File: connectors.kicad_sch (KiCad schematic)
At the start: 4 parts, among them J2 Conn_01x02, J3 Conn_01x02, J6 Conn_01x04, J7 Conn_01x04

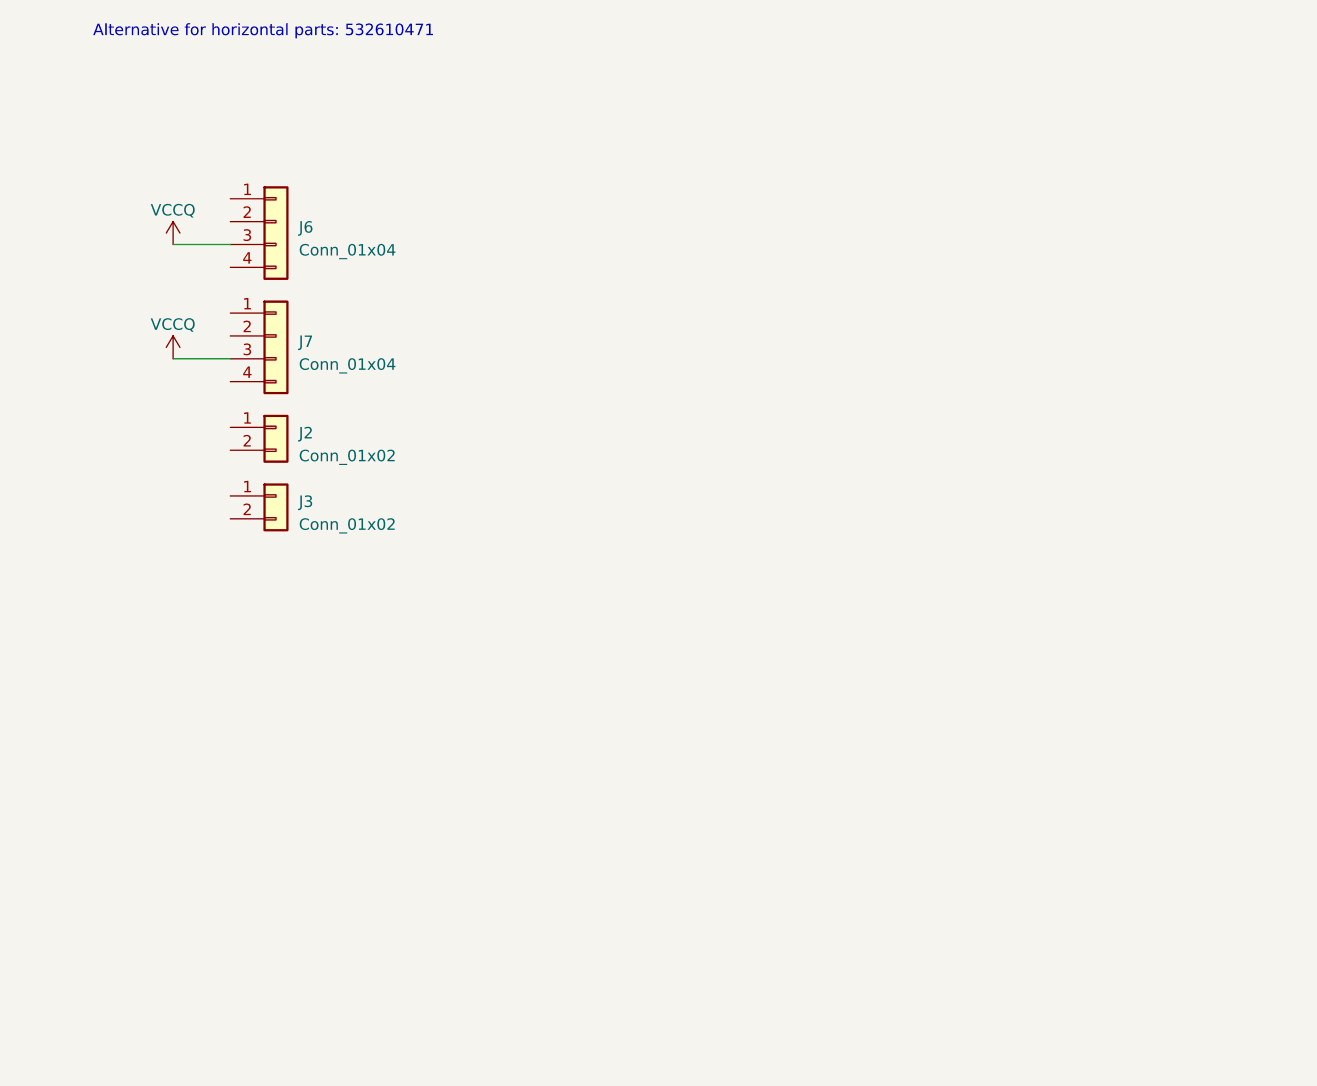
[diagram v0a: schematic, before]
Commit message: Add connections between existing sheets
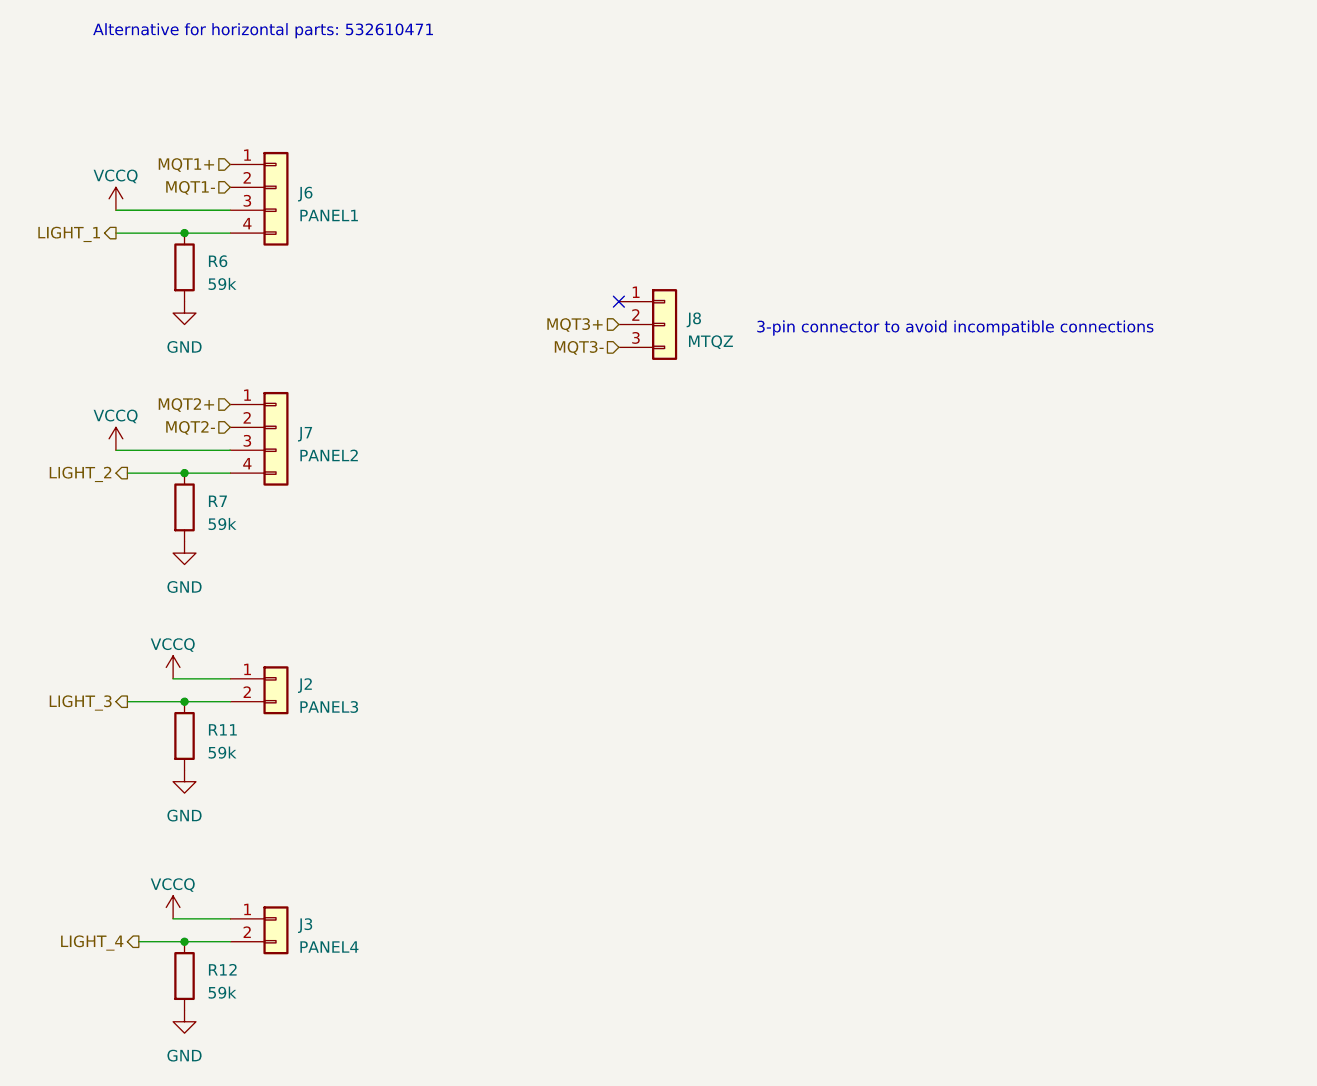
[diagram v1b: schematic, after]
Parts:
- added J8: MTQZ, Connector_Molex:Molex_PicoBlade_53398-0371_1x03-1MP_P1.25mm_Vertical, symbol Connector_Generic:Conn_01x03
- added R11, R12, R6, R7: 59k, LED_SMD:LED_0805_2012Metric_Pad1.15x1.40mm_HandSolder, symbol Device:R
- J2: value Conn_01x02 -> PANEL3; footprint (none) -> Connector_Molex:Molex_PicoBlade_53398-0271_1x02-1MP_P1.25mm_Vertical; MPN (none) -> 533980271
- J3: value Conn_01x02 -> PANEL4; footprint (none) -> Connector_Molex:Molex_PicoBlade_53398-0271_1x02-1MP_P1.25mm_Vertical; MPN (none) -> 533980271
- J6: value Conn_01x04 -> PANEL1; footprint (none) -> Connector_Molex:Molex_PicoBlade_53398-0471_1x04-1MP_P1.25mm_Vertical; MPN (none) -> 533980471
- J7: value Conn_01x04 -> PANEL2; footprint (none) -> Connector_Molex:Molex_PicoBlade_53398-0471_1x04-1MP_P1.25mm_Vertical; MPN (none) -> 533980471
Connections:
- net VCCQ: now also J2.1 (Pin_1), J3.1 (Pin_1)
- net MQT1+: now reaches J6.1 (Pin_1)
- net MQT1-: now reaches J6.2 (Pin_2)
- net LIGHT_1: now reaches J6.4 (Pin_4)
- net LIGHT_1: now also R6.1
- net LIGHT_3: now reaches J2.2 (Pin_2)
- net LIGHT_3: now also R11.1
- net MQT2+: now reaches J7.1 (Pin_1)
- net MQT2-: now reaches J7.2 (Pin_2)
- net LIGHT_2: now reaches J7.4 (Pin_4)
- net LIGHT_2: now also R7.1
- net LIGHT_4: now reaches J3.2 (Pin_2)
- net LIGHT_4: now also R12.1
- new net GND: R11.2, R12.2, R6.2, R7.2
- new net MQT3+: J8.2 (Pin_2)
- new net MQT3-: J8.3 (Pin_3)
- no-connect marks 0 -> 1
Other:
- note added: "3-pin connector to avoid incompatible connections"
- moved on the sheet: J2, J6

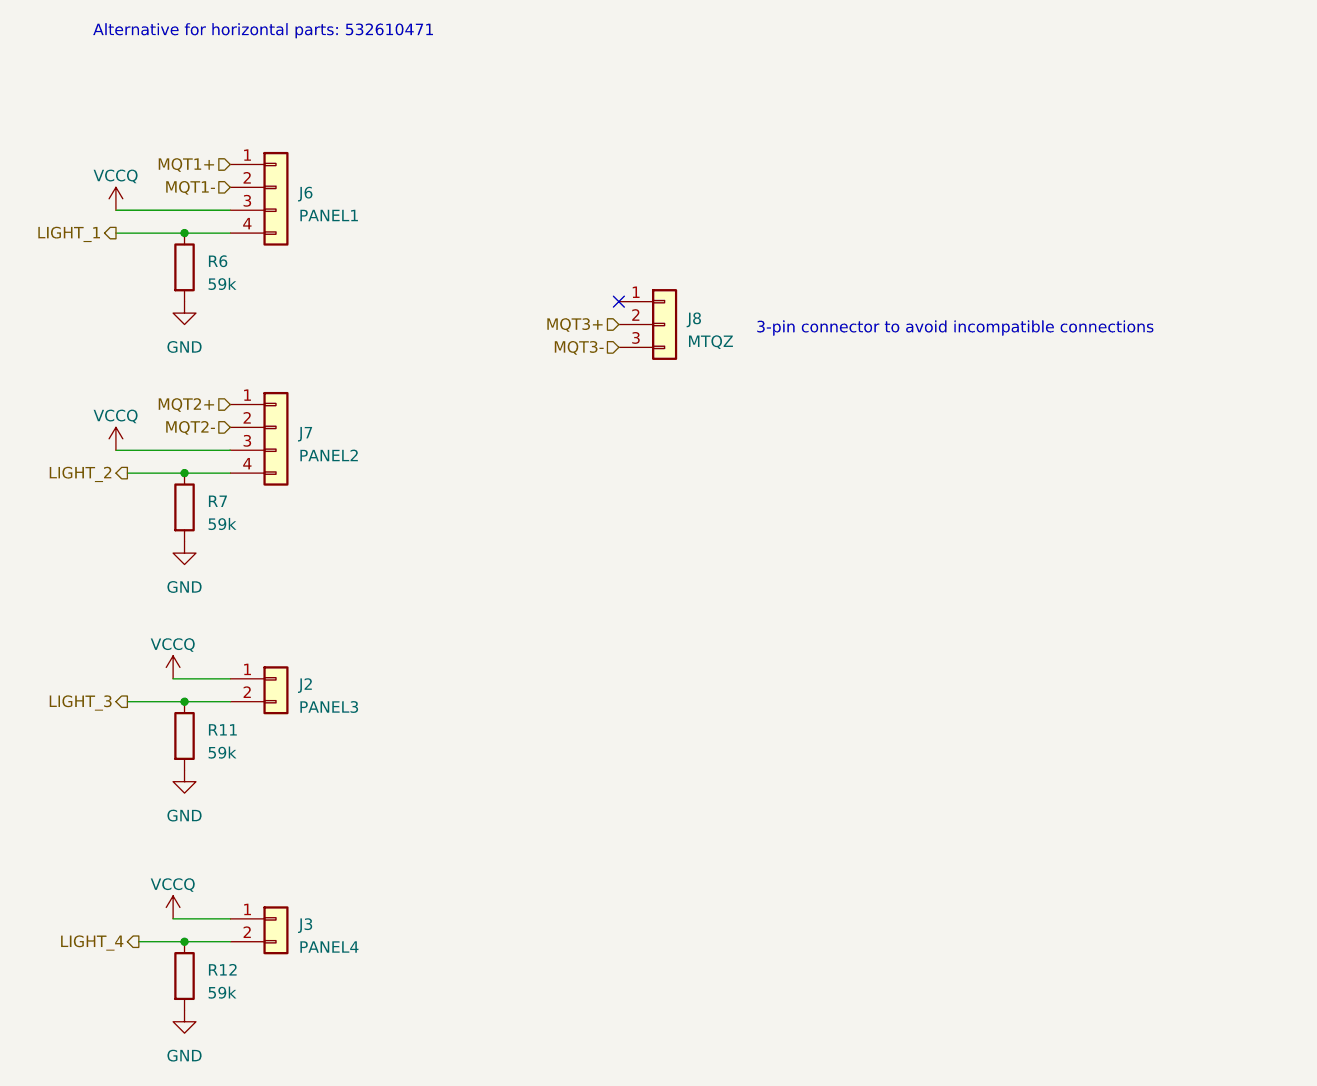
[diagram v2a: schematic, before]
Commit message: Reannotate schematic
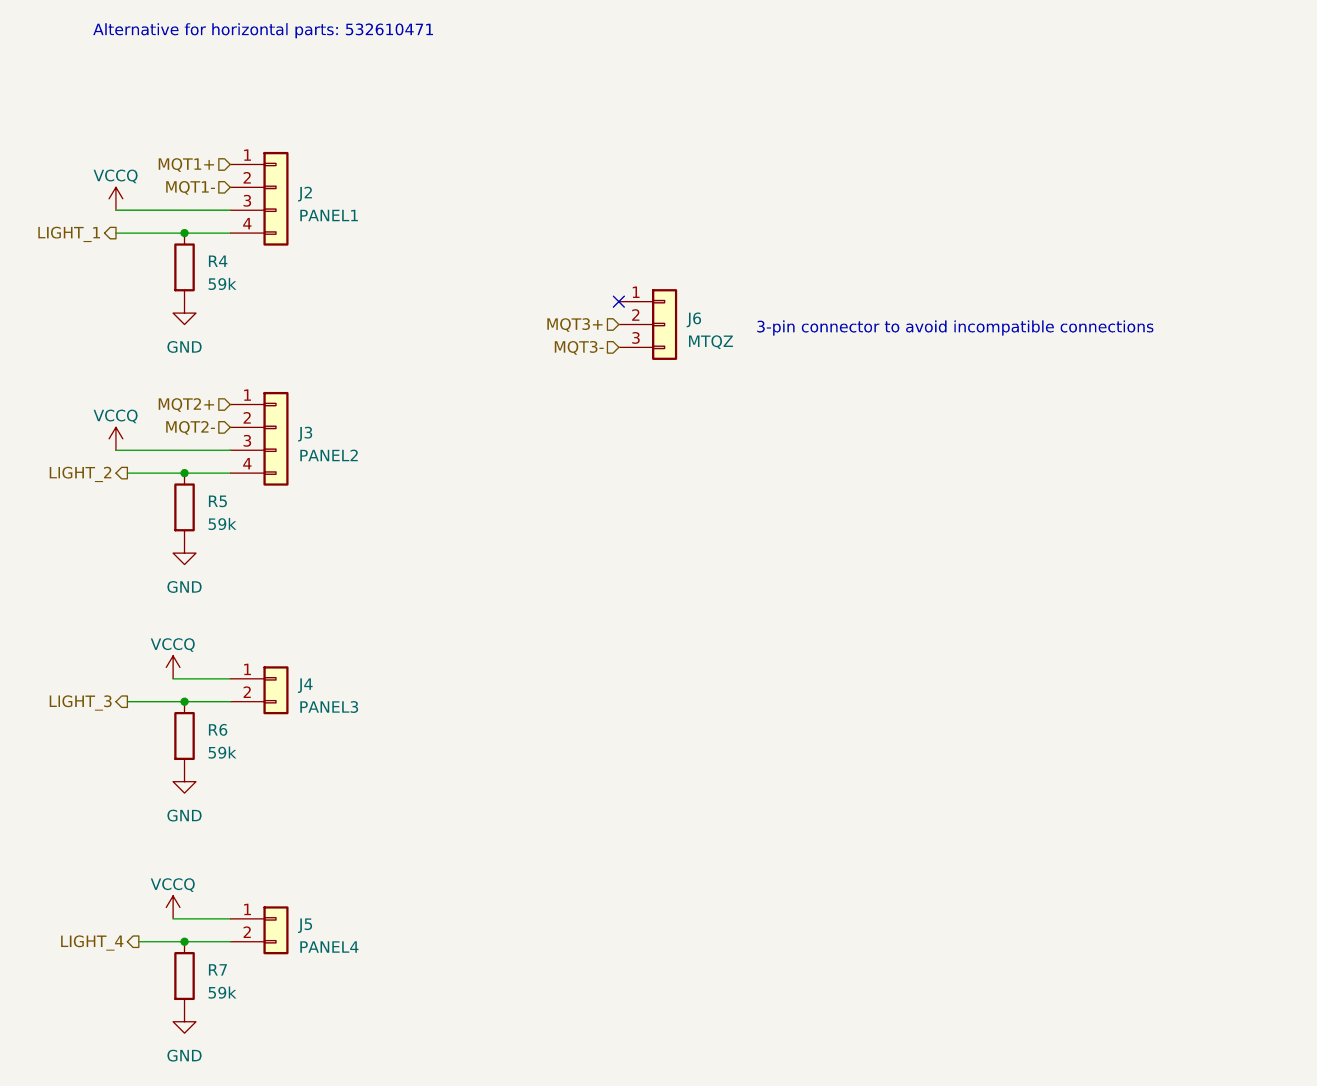
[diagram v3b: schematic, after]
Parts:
- renumbered J6 to J2, J7 to J3, J2 to J4, J3 to J5, J8 to J6, R6 to R4, R7 to R5, R11 to R6, R12 to R7
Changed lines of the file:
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@@
   (symbol (lib_id "Device:R") (at 116.84 67.31 0) (unit 1)
     (in_bom yes) (on_board yes) (dnp no) (fields_autoplaced)
-    (property "Reference" "R6" (at 119.38 66.675 0)
+    (property "Reference" "R4" (at 119.38 66.675 0)
       (effects (font (size 1.27 1.27)) (justify left))
     )
@@
       (project "NEW_PCB_ADCS"
         (path "/42c40d7d-71af-4ce9-bac9-d638f259c957/8584c500-e681-4774-8e2d-f320630e3d46"
-          (reference "R6") (unit 1)
+          (reference "R4") (unit 1)
         )
       )
@@
   (symbol (lib_id "Connector_Generic:Conn_01x03") (at 170.18 73.66 0) (unit 1)
     (in_bom yes) (on_board yes) (dnp no) (fields_autoplaced)
-    (property "Reference" "J8" (at 172.72 73.025 0)
+    (property "Reference" "J6" (at 172.72 73.025 0)
       (effects (font (size 1.27 1.27)) (justify left))
     )
@@
       (project "NEW_PCB_ADCS"
         (path "/42c40d7d-71af-4ce9-bac9-d638f259c957/8584c500-e681-4774-8e2d-f320630e3d46"
-          (reference "J8") (unit 1)
+          (reference "J6") (unit 1)
         )
       )
@@
   (symbol (lib_id "Connector_Generic:Conn_01x04") (at 127 58.42 0) (unit 1)
     (in_bom yes) (on_board yes) (dnp no) (fields_autoplaced)
-    (property "Reference" "J6" (at 129.54 59.055 0)
+    (property "Reference" "J2" (at 129.54 59.055 0)
       (effects (font (size 1.27 1.27)) (justify left))
     )
@@
       (project "NEW_PCB_ADCS"
         (path "/42c40d7d-71af-4ce9-bac9-d638f259c957/8584c500-e681-4774-8e2d-f320630e3d46"
-          (reference "J6") (unit 1)
+          (reference "J2") (unit 1)
         )
       )
@@
   (symbol (lib_id "Device:R") (at 116.84 146.05 0) (unit 1)
     (in_bom yes) (on_board yes) (dnp no) (fields_autoplaced)
-    (property "Reference" "R12" (at 119.38 145.415 0)
+    (property "Reference" "R7" (at 119.38 145.415 0)
       (effects (font (size 1.27 1.27)) (justify left))
     )
@@
       (project "NEW_PCB_ADCS"
         (path "/42c40d7d-71af-4ce9-bac9-d638f259c957/8584c500-e681-4774-8e2d-f320630e3d46"
-          (reference "R12") (unit 1)
+          (reference "R7") (unit 1)
         )
       )
@@
   (symbol (lib_id "Connector_Generic:Conn_01x02") (at 127 113.03 0) (unit 1)
     (in_bom yes) (on_board yes) (dnp no) (fields_autoplaced)
-    (property "Reference" "J2" (at 129.54 113.665 0)
+    (property "Reference" "J4" (at 129.54 113.665 0)
       (effects (font (size 1.27 1.27)) (justify left))
     )
@@
       (project "NEW_PCB_ADCS"
         (path "/42c40d7d-71af-4ce9-bac9-d638f259c957/8584c500-e681-4774-8e2d-f320630e3d46"
-          (reference "J2") (unit 1)
+          (reference "J4") (unit 1)
         )
       )
@@
   (symbol (lib_id "Connector_Generic:Conn_01x02") (at 127 139.7 0) (unit 1)
     (in_bom yes) (on_board yes) (dnp no) (fields_autoplaced)
-    (property "Reference" "J3" (at 129.54 140.335 0)
+    (property "Reference" "J5" (at 129.54 140.335 0)
       (effects (font (size 1.27 1.27)) (justify left))
     )
@@
       (project "NEW_PCB_ADCS"
         (path "/42c40d7d-71af-4ce9-bac9-d638f259c957/8584c500-e681-4774-8e2d-f320630e3d46"
-          (reference "J3") (unit 1)
+          (reference "J5") (unit 1)
         )
       )
@@
   (symbol (lib_id "power:GND") (at 116.84 123.19 0) (unit 1)
     (in_bom yes) (on_board yes) (dnp no) (fields_autoplaced)
-    (property "Reference" "#PWR061" (at 116.84 129.54 0)
+    (property "Reference" "#PWR015" (at 116.84 129.54 0)
       (effects (font (size 1.27 1.27)) hide)
     )
@@
       (project "NEW_PCB_ADCS"
         (path "/42c40d7d-71af-4ce9-bac9-d638f259c957/8584c500-e681-4774-8e2d-f320630e3d46"
-          (reference "#PWR061") (unit 1)
+          (reference "#PWR015") (unit 1)
         )
       )
@@
   (symbol (lib_id "power:VCCQ") (at 115.57 139.7 0) (unit 1)
     (in_bom yes) (on_board yes) (dnp no) (fields_autoplaced)
-    (property "Reference" "#PWR066" (at 115.57 143.51 0)
+    (property "Reference" "#PWR012" (at 115.57 143.51 0)
       (effects (font (size 1.27 1.27)) hide)
     )
@@
       (project "NEW_PCB_ADCS"
         (path "/42c40d7d-71af-4ce9-bac9-d638f259c957/8584c500-e681-4774-8e2d-f320630e3d46"
-          (reference "#PWR066") (unit 1)
+          (reference "#PWR012") (unit 1)
         )
       )
@@
   (symbol (lib_id "power:VCCQ") (at 109.22 87.63 0) (unit 1)
     (in_bom yes) (on_board yes) (dnp no) (fields_autoplaced)
-    (property "Reference" "#PWR065" (at 109.22 91.44 0)
+    (property "Reference" "#PWR010" (at 109.22 91.44 0)
       (effects (font (size 1.27 1.27)) hide)
     )
@@
       (project "NEW_PCB_ADCS"
         (path "/42c40d7d-71af-4ce9-bac9-d638f259c957/8584c500-e681-4774-8e2d-f320630e3d46"
-          (reference "#PWR065") (unit 1)
+          (reference "#PWR010") (unit 1)
         )
       )
@@
   (symbol (lib_id "power:VCCQ") (at 115.57 113.03 0) (unit 1)
     (in_bom yes) (on_board yes) (dnp no) (fields_autoplaced)
-    (property "Reference" "#PWR067" (at 115.57 116.84 0)
+    (property "Reference" "#PWR011" (at 115.57 116.84 0)
       (effects (font (size 1.27 1.27)) hide)
     )
@@
       (project "NEW_PCB_ADCS"
         (path "/42c40d7d-71af-4ce9-bac9-d638f259c957/8584c500-e681-4774-8e2d-f320630e3d46"
-          (reference "#PWR067") (unit 1)
+          (reference "#PWR011") (unit 1)
         )
       )
@@
   (symbol (lib_id "power:GND") (at 116.84 149.86 0) (unit 1)
     (in_bom yes) (on_board yes) (dnp no) (fields_autoplaced)
-    (property "Reference" "#PWR062" (at 116.84 156.21 0)
+    (property "Reference" "#PWR016" (at 116.84 156.21 0)
       (effects (font (size 1.27 1.27)) hide)
     )
@@
       (project "NEW_PCB_ADCS"
         (path "/42c40d7d-71af-4ce9-bac9-d638f259c957/8584c500-e681-4774-8e2d-f320630e3d46"
-          (reference "#PWR062") (unit 1)
+          (reference "#PWR016") (unit 1)
         )
       )
@@
   (symbol (lib_id "power:GND") (at 116.84 71.12 0) (unit 1)
     (in_bom yes) (on_board yes) (dnp no) (fields_autoplaced)
-    (property "Reference" "#PWR058" (at 116.84 77.47 0)
+    (property "Reference" "#PWR013" (at 116.84 77.47 0)
       (effects (font (size 1.27 1.27)) hide)
     )
@@
       (project "NEW_PCB_ADCS"
         (path "/42c40d7d-71af-4ce9-bac9-d638f259c957/8584c500-e681-4774-8e2d-f320630e3d46"
-          (reference "#PWR058") (unit 1)
+          (reference "#PWR013") (unit 1)
         )
       )
@@
   (symbol (lib_id "power:VCCQ") (at 109.22 60.96 0) (unit 1)
     (in_bom yes) (on_board yes) (dnp no) (fields_autoplaced)
-    (property "Reference" "#PWR064" (at 109.22 64.77 0)
+    (property "Reference" "#PWR09" (at 109.22 64.77 0)
       (effects (font (size 1.27 1.27)) hide)
     )
@@
       (project "NEW_PCB_ADCS"
         (path "/42c40d7d-71af-4ce9-bac9-d638f259c957/8584c500-e681-4774-8e2d-f320630e3d46"
-          (reference "#PWR064") (unit 1)
+          (reference "#PWR09") (unit 1)
         )
       )
@@
   (symbol (lib_id "Device:R") (at 116.84 93.98 0) (unit 1)
     (in_bom yes) (on_board yes) (dnp no) (fields_autoplaced)
-    (property "Reference" "R7" (at 119.38 93.345 0)
+    (property "Reference" "R5" (at 119.38 93.345 0)
       (effects (font (size 1.27 1.27)) (justify left))
     )
@@
       (project "NEW_PCB_ADCS"
         (path "/42c40d7d-71af-4ce9-bac9-d638f259c957/8584c500-e681-4774-8e2d-f320630e3d46"
-          (reference "R7") (unit 1)
+          (reference "R5") (unit 1)
         )
       )
@@
   (symbol (lib_id "Connector_Generic:Conn_01x04") (at 127 85.09 0) (unit 1)
     (in_bom yes) (on_board yes) (dnp no) (fields_autoplaced)
-    (property "Reference" "J7" (at 129.54 85.725 0)
+    (property "Reference" "J3" (at 129.54 85.725 0)
       (effects (font (size 1.27 1.27)) (justify left))
     )
@@
       (project "NEW_PCB_ADCS"
         (path "/42c40d7d-71af-4ce9-bac9-d638f259c957/8584c500-e681-4774-8e2d-f320630e3d46"
-          (reference "J7") (unit 1)
+          (reference "J3") (unit 1)
         )
       )
@@
   (symbol (lib_id "power:GND") (at 116.84 97.79 0) (unit 1)
     (in_bom yes) (on_board yes) (dnp no) (fields_autoplaced)
-    (property "Reference" "#PWR060" (at 116.84 104.14 0)
+    (property "Reference" "#PWR014" (at 116.84 104.14 0)
       (effects (font (size 1.27 1.27)) hide)
     )
@@
       (project "NEW_PCB_ADCS"
         (path "/42c40d7d-71af-4ce9-bac9-d638f259c957/8584c500-e681-4774-8e2d-f320630e3d46"
-          (reference "#PWR060") (unit 1)
+          (reference "#PWR014") (unit 1)
         )
       )
@@
   (symbol (lib_id "Device:R") (at 116.84 119.38 0) (unit 1)
     (in_bom yes) (on_board yes) (dnp no) (fields_autoplaced)
-    (property "Reference" "R11" (at 119.38 118.745 0)
+    (property "Reference" "R6" (at 119.38 118.745 0)
       (effects (font (size 1.27 1.27)) (justify left))
     )
@@
       (project "NEW_PCB_ADCS"
         (path "/42c40d7d-71af-4ce9-bac9-d638f259c957/8584c500-e681-4774-8e2d-f320630e3d46"
-          (reference "R11") (unit 1)
-        )
-      )
+          (reference "R6") (unit 1)
+        )
+      )
